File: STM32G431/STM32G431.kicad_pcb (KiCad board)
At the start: 4 copper layers, 60 x 44 mm, 155 parts, among them J1 W, J10 NTC, J11 LED, J2 U, J3 V, J4 GND, J5 VIN, J6 UART, J8 HALL, J9 AIN/PWM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

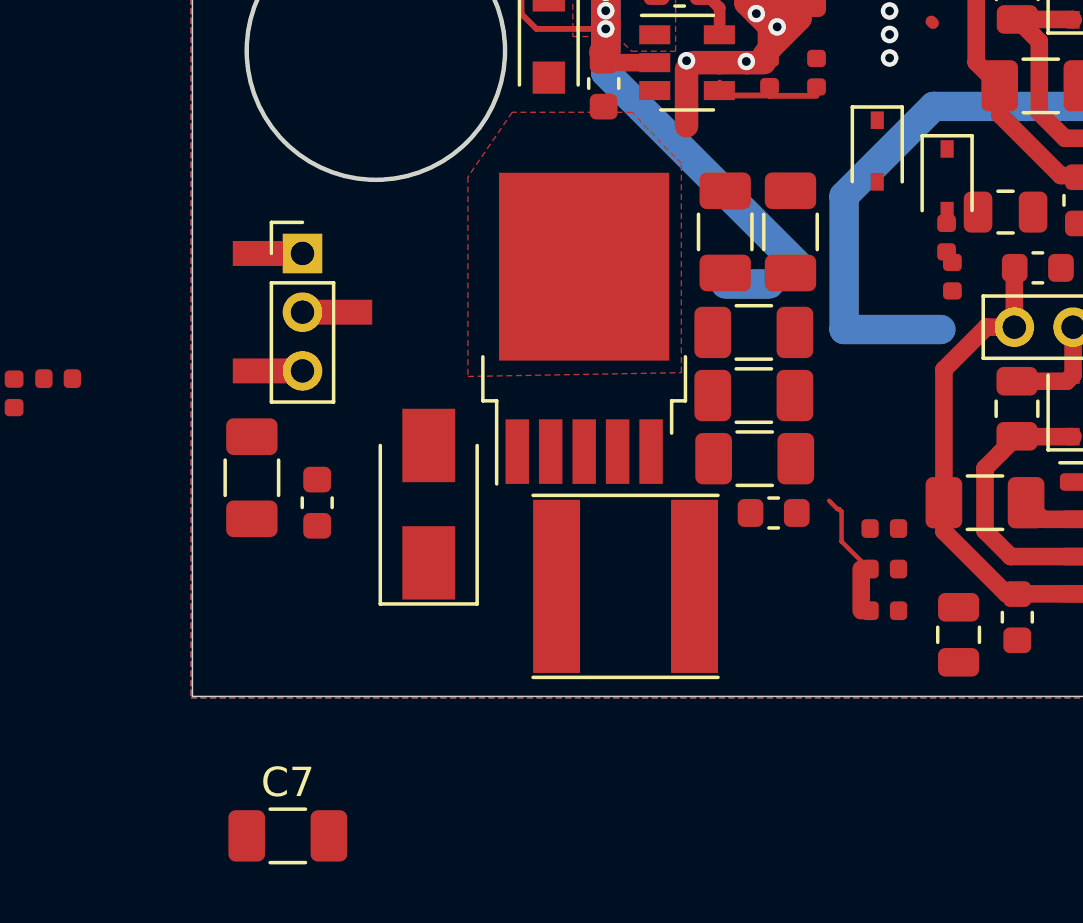
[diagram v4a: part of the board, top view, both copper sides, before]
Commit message: updated layout
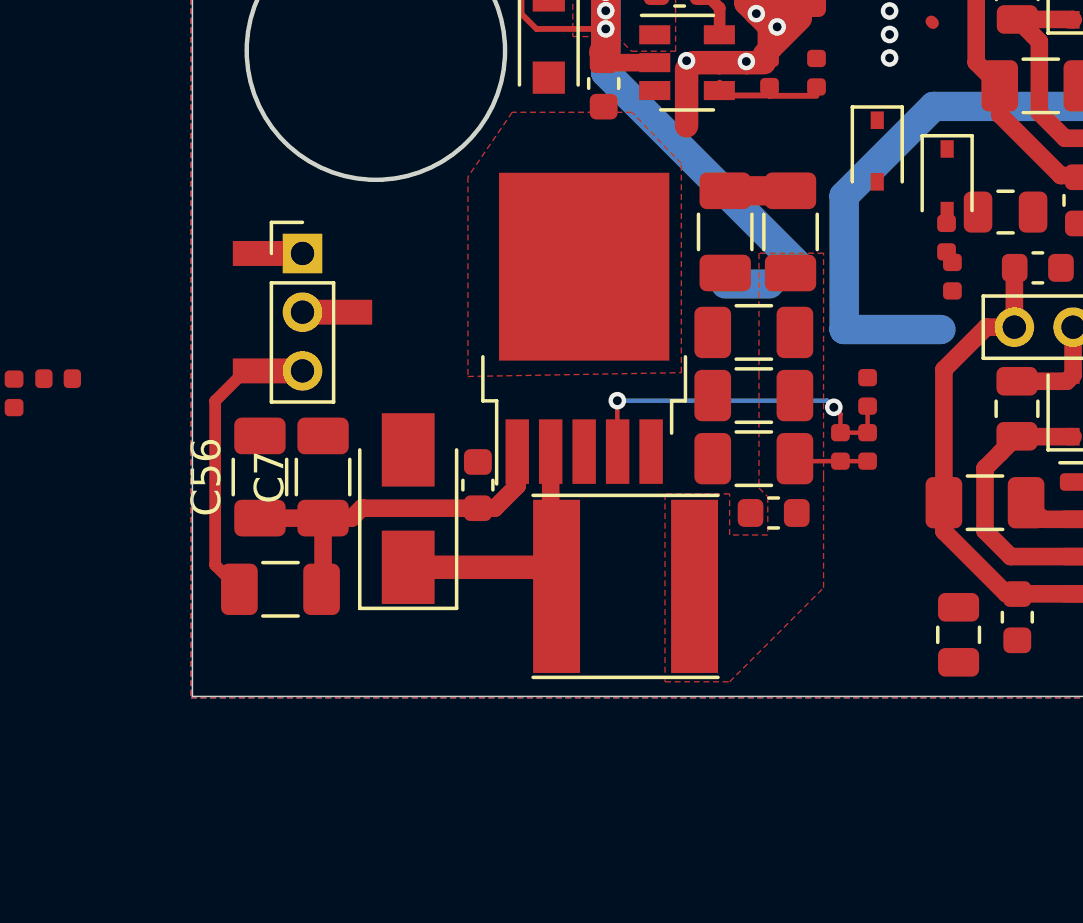
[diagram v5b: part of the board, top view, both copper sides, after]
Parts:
- added C56: 10u, Capacitor_SMD:C_1206_3216Metric, F.Cu at (22.3, 59.5)
- moved C7 12.3 mm to (24.4, 59.5), turned to 90 degrees
- moved R1 5.61 mm to (43.0, 58.5), turned to 270 degrees
- moved C21 5.51 mm to (29.7, 59.8)
- moved R7 4.69 mm to (43.0, 56.6), turned to 270 degrees
- moved C20 4.42 mm to (42.1, 58.5), turned to 90 degrees
- moved R44 3.92 mm to (23.0, 63.4), turned to 0 degrees
- moved D1 0.72 mm to (27.4, 60.6)
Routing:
- net Net-(C21-Pad1): track 0.00 -> 12.8 mm
- net Net-(C20-Pad2): track 0.00 -> 12.0 mm, vias 0 -> 2
- net Net-(D1-Pad1): track 0.00 -> 10.00 mm
- net VIN: track 1.20 -> 10.2 mm
- net Net-(C53-Pad1): track 0.00 -> 2.23 mm
- net +12V: track 100.9 -> 99.2 mm
- added copper zone on F.Cu, net +12V

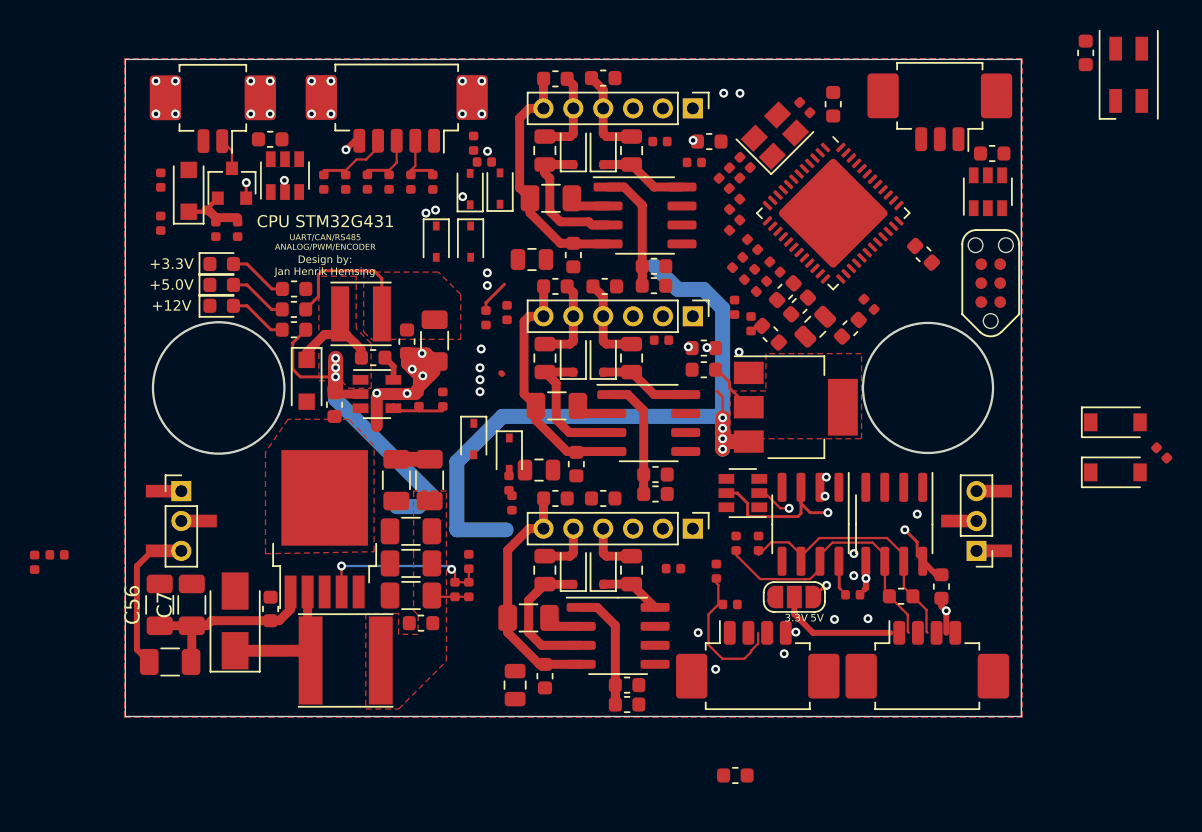
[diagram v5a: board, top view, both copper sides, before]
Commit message: updated layout
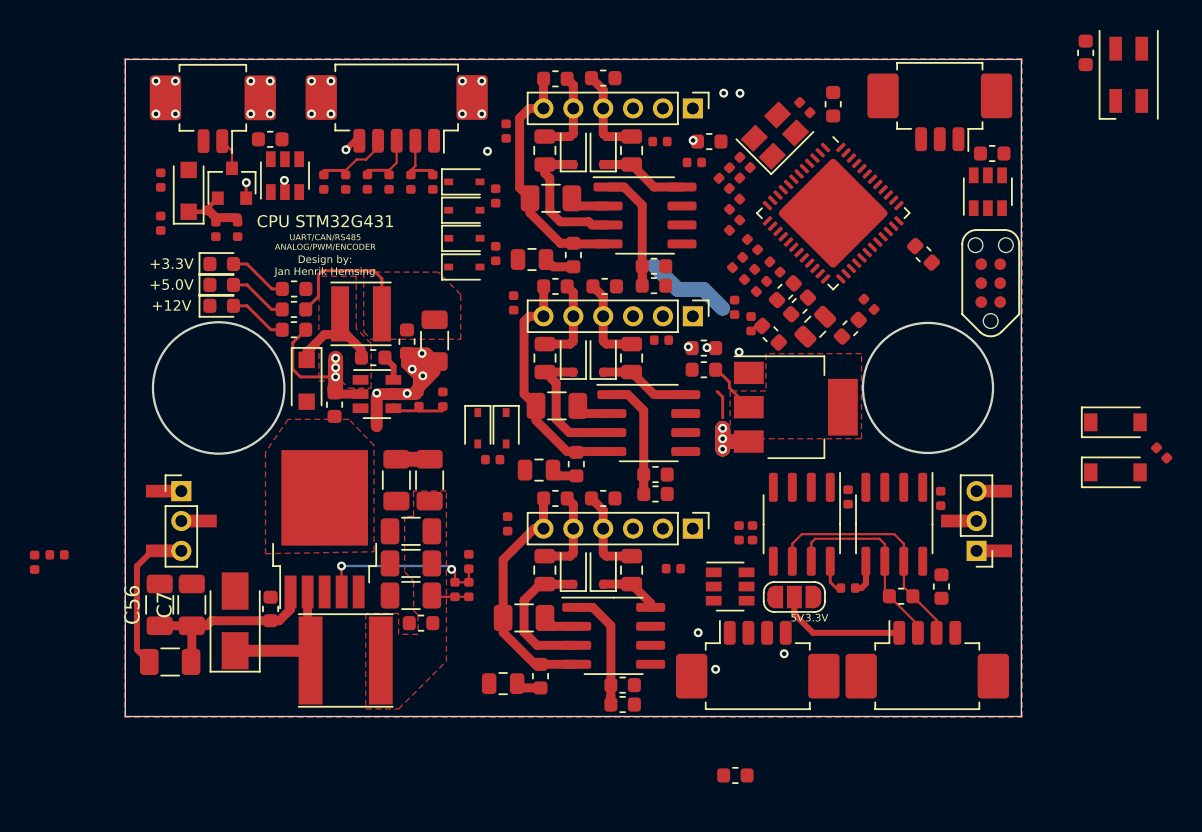
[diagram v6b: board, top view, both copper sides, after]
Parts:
- moved R5 12.6 mm to (74.6, 52.4)
- moved R4 8.12 mm to (68.4, 52.3)
- moved U11 6.32 mm to (60.5, 58.3), turned to 0 degrees
- moved R46 5.03 mm to (62.0, 54.7), turned to 90 degrees
- moved R26 4.35 mm to (44.8, 36.0)
- moved R45 2.99 mm to (61.1, 54.7)
- moved D13 2.80 mm to (42.7, 33.1), turned to 0 degrees
- moved D6 2.53 mm to (42.7, 36.9), turned to 0 degrees
- moved R31 2.39 mm to (44.8, 32.1), turned to 90 degrees
- moved R30 2.33 mm to (45.5, 27.8)
- moved R24 1.91 mm to (44.6, 49.8), turned to 0 degrees
- moved D2 1.71 mm to (45.5, 47.7)
- moved R23 1.43 mm to (45.6, 54.1), turned to 90 degrees
- moved C50 0.81 mm to (45.3, 64.8), turned to 0 degrees
- moved R25 0.78 mm to (46.0, 39.3), turned to 90 degrees
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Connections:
- J9 pad 3: Net-(J9-Pad3) -> AinC
- R45 pad 2: Net-(J9-Pad3) -> AinC
- R46 pad 2: Net-(J9-Pad3) -> AinC
- U11 pad 4: Net-(U11-Pad4) -> AinC
- U11 pad 6: Ain -> Net-(U11-Pad6)
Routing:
- net +12V: track 99.2 -> 51.2 mm, vias 7 -> 6
- net +5V: track 35.9 -> 9.62 mm, vias 3 -> 0
- net Net-(J9-Pad3): track 9.37 -> 0.00 mm
- net CANH: track 18.4 -> 13.2 mm
- net GND: track 31.2 -> 26.7 mm, vias 53 -> 34
- net Net-(C3-Pad1): track 3.62 -> 5.96 mm
- net Net-(C2-Pad2): track 3.63 -> 5.82 mm
- net Net-(C52-Pad2): track 0.00 -> 2.03 mm
- net Net-(D7-Pad2): track 1.97 -> 0.00 mm
- net CANL: track 17.4 -> 15.4 mm
- net Net-(C50-Pad2): track 0.00 -> 1.68 mm
- net Net-(C51-Pad2): track 0.08 -> 1.72 mm, vias 1 -> 0
- net Net-(J6-Pad1): track 8.09 -> 8.69 mm

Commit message: updated layout
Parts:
- moved D17 13.5 mm to (76.2, 31.8), turned to 0 degrees
- moved U8 7.59 mm to (73.9, 38.4), turned to 180 degrees
- moved C43 7.14 mm to (60.5, 50.7)
- moved R14 3.38 mm to (59.7, 36.4), turned to 225 degrees
- moved C46 3.28 mm to (59.6, 45.5), turned to 90 degrees
- moved R23 1.02 mm to (45.8, 53.1)
- moved R8 0.67 mm to (61.6, 40.1), turned to 225 degrees
- moved C9 0.65 mm to (73.5, 35.4), turned to 0 degrees
- moved C55 0.30 mm to (78.1, 29.0)
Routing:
- net +12V: track 51.2 -> 45.6 mm
- net +3V3: track 3.64 -> 2.15 mm
- net GND: vias 34 -> 31

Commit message: updated layout
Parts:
- moved C4 0.10 mm to (65.4, 26.2)
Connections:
- U8 pad 5: +5V -> +3V3
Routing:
- net SWDIO: track 0.00 -> 11.6 mm
- net +3V3: track 2.15 -> 11.9 mm
- net SWCLK: track 0.00 -> 9.64 mm
- net NRST: track 0.00 -> 6.50 mm, vias 0 -> 2
- net Net-(C4-Pad1): track 0.00 -> 6.23 mm
- net IUH: track 0.00 -> 5.55 mm
- net IVH: track 0.00 -> 4.46 mm
- net IWH: track 0.00 -> 4.46 mm
- net Net-(C5-Pad1): track 0.00 -> 4.08 mm
- net Vin_mon: track 0.00 -> 3.45 mm
- net IWL: track 0.00 -> 3.43 mm
- net UU: track 0.00 -> 3.13 mm
- net VDDA: track 0.00 -> 3.06 mm
- net UV: track 0.00 -> 2.98 mm
- net UW: track 0.00 -> 2.26 mm
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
